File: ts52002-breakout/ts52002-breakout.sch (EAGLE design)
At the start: 23 parts, among them U1 TS52002

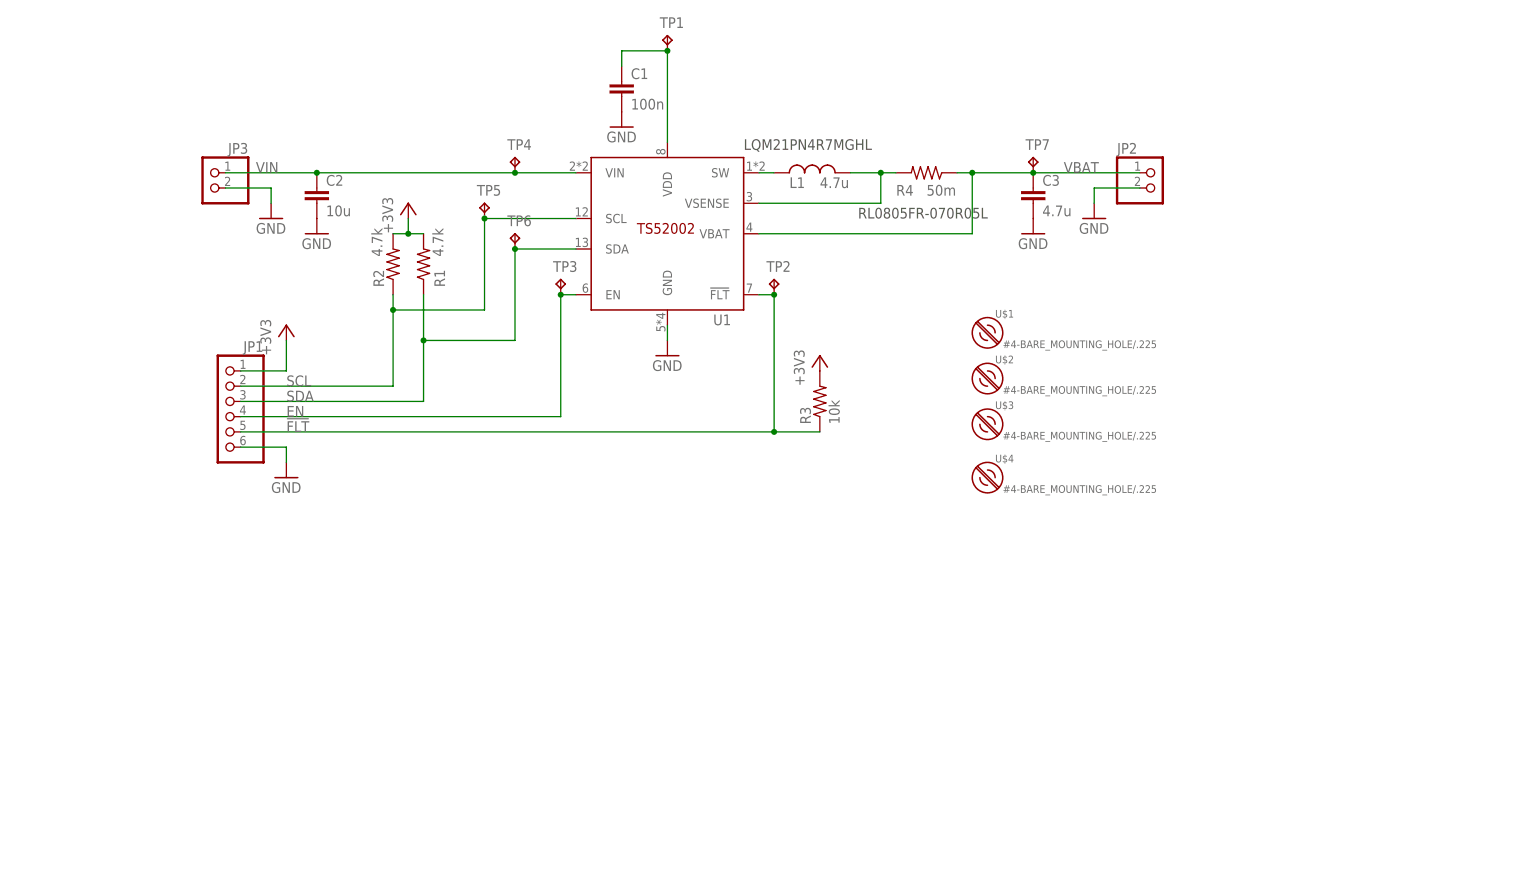
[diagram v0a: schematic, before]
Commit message: Better inductor, and better labeling. Sent to OSH Park!
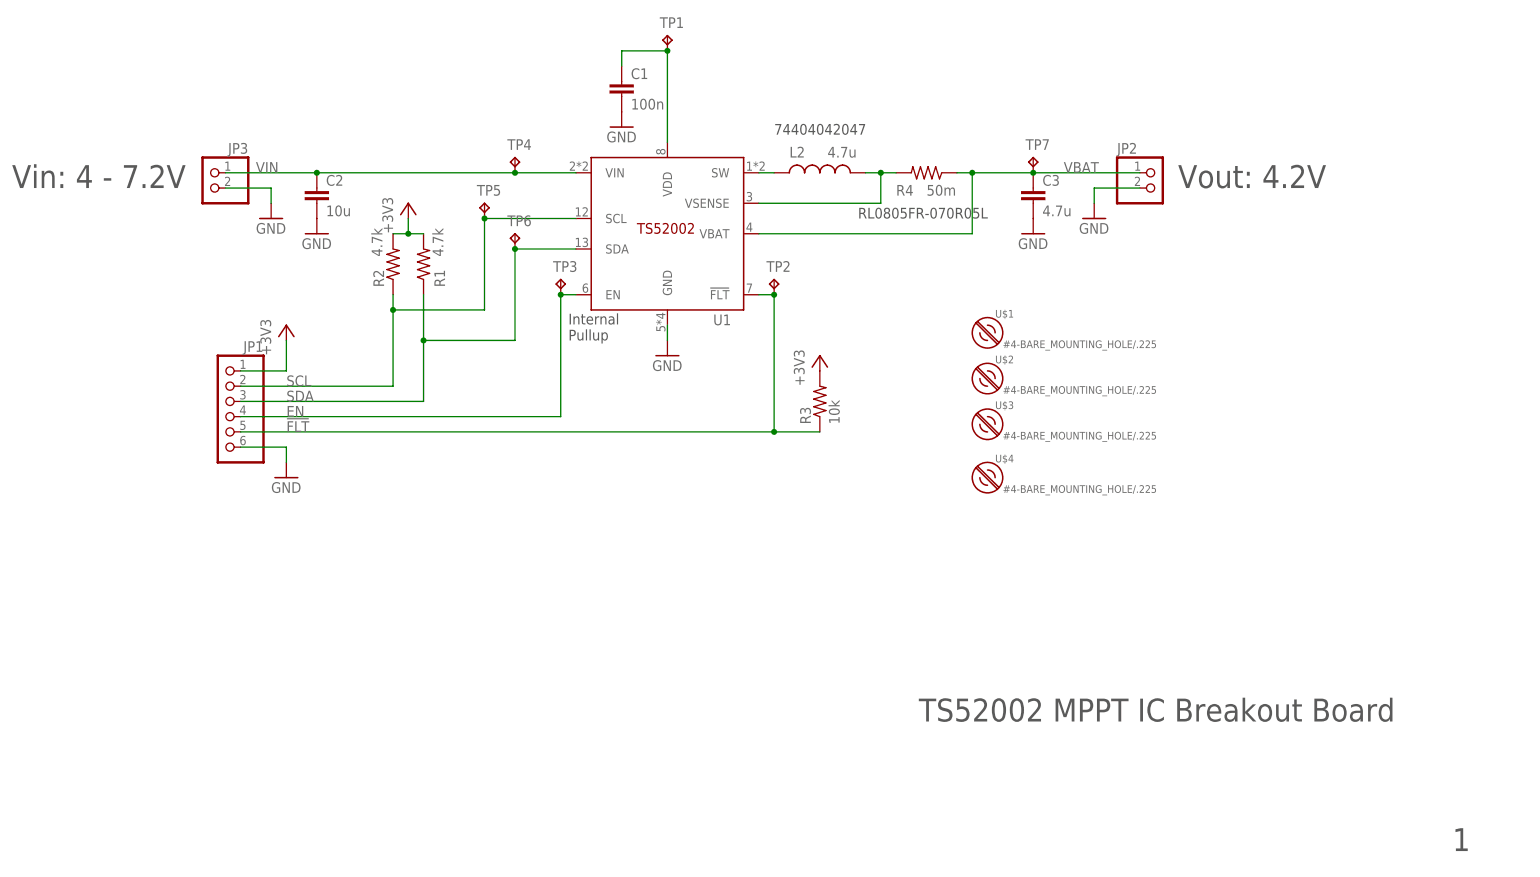
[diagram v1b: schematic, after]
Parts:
- removed L1: 4.7u, rcl_custom:L-US0805-B-NOSILK
- added L2: 4.7u, wurth-4518-inductor:WURTH-4518-INDUCTOR
- C2, C3: device rcl_custom:C-EU0603-B-NOSILK -> rcl_custom:C-EU0805-B-NOSILK
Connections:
- net SW: now also L2.1; no longer L1.1
- net VSENSE: now also L2.2; no longer L1.2
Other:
- note added: "1"
- note added: "74404042047"
- note added: "Internal Pullup"
- note added: "TS52002 MPPT IC Breakout Board"
- note added: "Vin: 4 - 7.2V"
- note added: "Vout: 4.2V"
- note removed: "LQM21PN4R7MGHL"
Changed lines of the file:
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@@
 <setting verticaltext="up"/>
 </settings>
-<grid distance="0.05" unitdist="inch" unit="inch" style="lines" multiple="2" display="no" altdistance="0.01" altunitdist="inch" altunit="inch"/>
+<grid distance="0.05" unitdist="inch" unit="inch" style="lines" multiple="2" display="yes" altdistance="0.01" altunitdist="inch" altunit="inch"/>
 <layers>
 <layer number="1" name="Top" color="4" fill="1" visible="no" active="no"/>
@@
 <part name="+3V4" library="supply1" library_urn="urn:adsk.eagle:library:371" deviceset="+3V3" device=""/>
 <part name="JP1" library="pinhead" library_urn="urn:adsk.eagle:library:325" deviceset="PINHD-1X6" device="" package3d_urn="urn:adsk.eagle:package:22472/2"/>
-<part name="C2" library="rcl_custom" deviceset="C-EU" device="0603-B-NOSILK" value="10u"/>
-<part name="C3" library="rcl_custom" deviceset="C-EU" device="0603-B-NOSILK" value="4.7u"/>
+<part name="C2" library="rcl_custom" deviceset="C-EU" device="0805-B-NOSILK" value="10u"/>
+<part name="C3" library="rcl_custom" deviceset="C-EU" device="0805-B-NOSILK" value="4.7u"/>
 <part name="GND6" library="supply1" library_urn="urn:adsk.eagle:library:371" deviceset="GND" device=""/>
 <part name="GND7" library="supply1" library_urn="urn:adsk.eagle:library:371" deviceset="GND" device=""/>
@@
 <part name="TP6" library="testpad" library_urn="urn:adsk.eagle:library:385" deviceset="TP" device="PAD1-13" package3d_urn="urn:adsk.eagle:package:27946/1"/>
 <part name="R4" library="rcl_custom" deviceset="R-US_" device="0805-B-NOSILK" value="50m"/>
-<part name="L1" library="rcl_custom" deviceset="L-US" device="0805-B-NOSILK" value="4.7u"/>
 <part name="TP7" library="testpad" library_urn="urn:adsk.eagle:library:385" deviceset="TP" device="PAD1-13" package3d_urn="urn:adsk.eagle:package:27946/1"/>
 <part name="U$1" library="mount" deviceset="#4-BARE_MOUNTING_HOLE" device="/.225"/>
@@
 <part name="U$3" library="mount" deviceset="#4-BARE_MOUNTING_HOLE" device="/.225"/>
 <part name="U$4" library="mount" deviceset="#4-BARE_MOUNTING_HOLE" device="/.225"/>
+<part name="L2" library="wurth-4518-inductor" deviceset="WURTH-4518-INDUCTOR" device="" value="4.7u"/>
 </parts>
 <sheets>
 <sheet>
 <plain>
-<text x="147.32" y="123.19" size="1.778" layer="97">LQM21PN4R7MGHL</text>
+<text x="152.4" y="125.73" size="1.778" layer="97">74404042047</text>
 <text x="166.37" y="111.76" size="1.778" layer="97">RL0805FR-070R05L</text>
+<text x="176.53" y="27.94" size="3.81" layer="97">TS52002 MPPT IC Breakout Board</text>
+<text x="265.43" y="6.35" size="3.81" layer="97">1</text>
+<text x="25.4" y="116.84" size="3.81" layer="97">Vin: 4 - 7.2V</text>
+<text x="219.71" y="116.84" size="3.81" layer="97">Vout: 4.2V</text>
+<text x="118.11" y="91.44" size="1.778" layer="97">Internal
+Pullup</text>
 </plain>
 <instances>
@@
 <attribute name="VALUE" x="177.8" y="115.57" size="1.778" layer="96"/>
 </instance>
-<instance part="L1" gate="L" x="160.02" y="119.38" smashed="yes">
-<attribute name="NAME" x="154.94" y="116.84" size="1.778" layer="95"/>
-<attribute name="VALUE" x="160.02" y="116.84" size="1.778" layer="96" rot="MR180" align="top-left"/>
-</instance>
 <instance part="TP7" gate="G$1" x="195.58" y="121.92"/>
 <instance part="U$1" gate="MT" x="187.96" y="92.71"/>
@@
 <instance part="U$3" gate="MT" x="187.96" y="77.47"/>
 <instance part="U$4" gate="MT" x="187.96" y="68.58"/>
+<instance part="L2" gate="G$1" x="160.02" y="119.38" smashed="yes" rot="R90">
+<attribute name="NAME" x="154.94" y="121.92" size="1.778" layer="95"/>
+<attribute name="VALUE" x="161.29" y="121.92" size="1.778" layer="96"/>
+</instance>
 </instances>
 <busses>
@@
 <pinref part="U1" gate="G$1" pin="SW"/>
 <wire x1="149.86" y1="119.38" x2="152.4" y2="119.38" width="0.1524" layer="91"/>
-<pinref part="L1" gate="L" pin="1"/>
+<pinref part="L2" gate="G$1" pin="1"/>
 </segment>
 </net>
@@
 <wire x1="149.86" y1="114.3" x2="170.18" y2="114.3" width="0.1524" layer="91"/>
 <wire x1="170.18" y1="114.3" x2="170.18" y2="119.38" width="0.1524" layer="91"/>
-<wire x1="170.18" y1="119.38" x2="165.1" y2="119.38" width="0.1524" layer="91"/>
-<junction x="170.18" y="119.38"/>
 <pinref part="R4" gate="R" pin="2"/>
 <wire x1="170.18" y1="119.38" x2="172.72" y2="119.38" width="0.1524" layer="91"/>
-<pinref part="L1" gate="L" pin="2"/>
+<pinref part="L2" gate="G$1" pin="2"/>
+<wire x1="167.64" y1="119.38" x2="170.18" y2="119.38" width="0.1524" layer="91"/>
+<junction x="170.18" y="119.38"/>
 </segment>
 </net>
@@
 </drawing>
 <compatibility>
+<note version="6.3" minversion="6.2.2" severity="warning">
+Since Version 6.2.2 text objects can contain more than one line,
+which will not be processed correctly with this version.
+</note>
 <note version="8.2" severity="warning">
 Since Version 8.2, EAGLE supports online libraries. The ids
